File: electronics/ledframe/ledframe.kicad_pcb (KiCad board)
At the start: 2 copper layers, 31 parts, among them CON1 BARREL_JACK, IC1 ATMEGA328P-AUR, P1 PIEZO_IN, P2 FTDI, P3 ICSP, P4 LED_WS2812b, P5 ANT, P6 CONN_01X08, Q1 BSS138, Q2 BSS138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

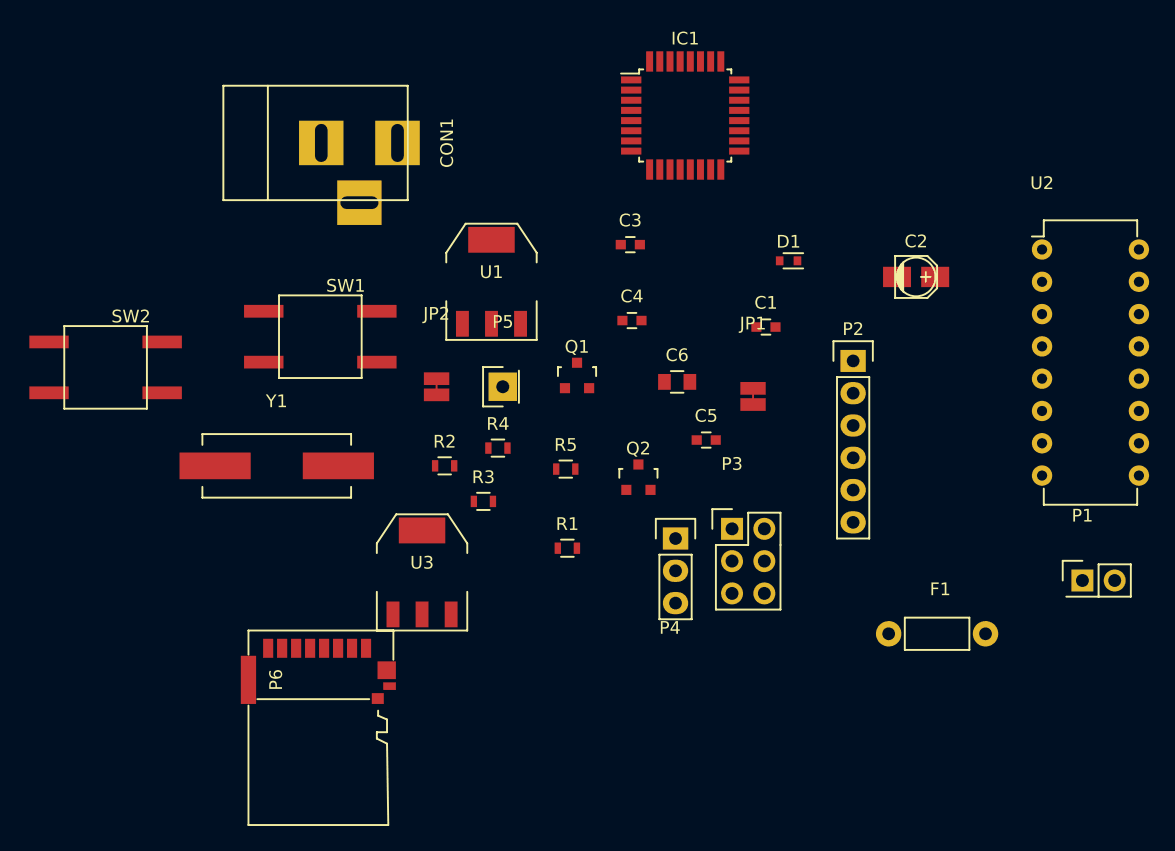
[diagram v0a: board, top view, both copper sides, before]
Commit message: draft layout. still needs rfm69 and resonator footprints
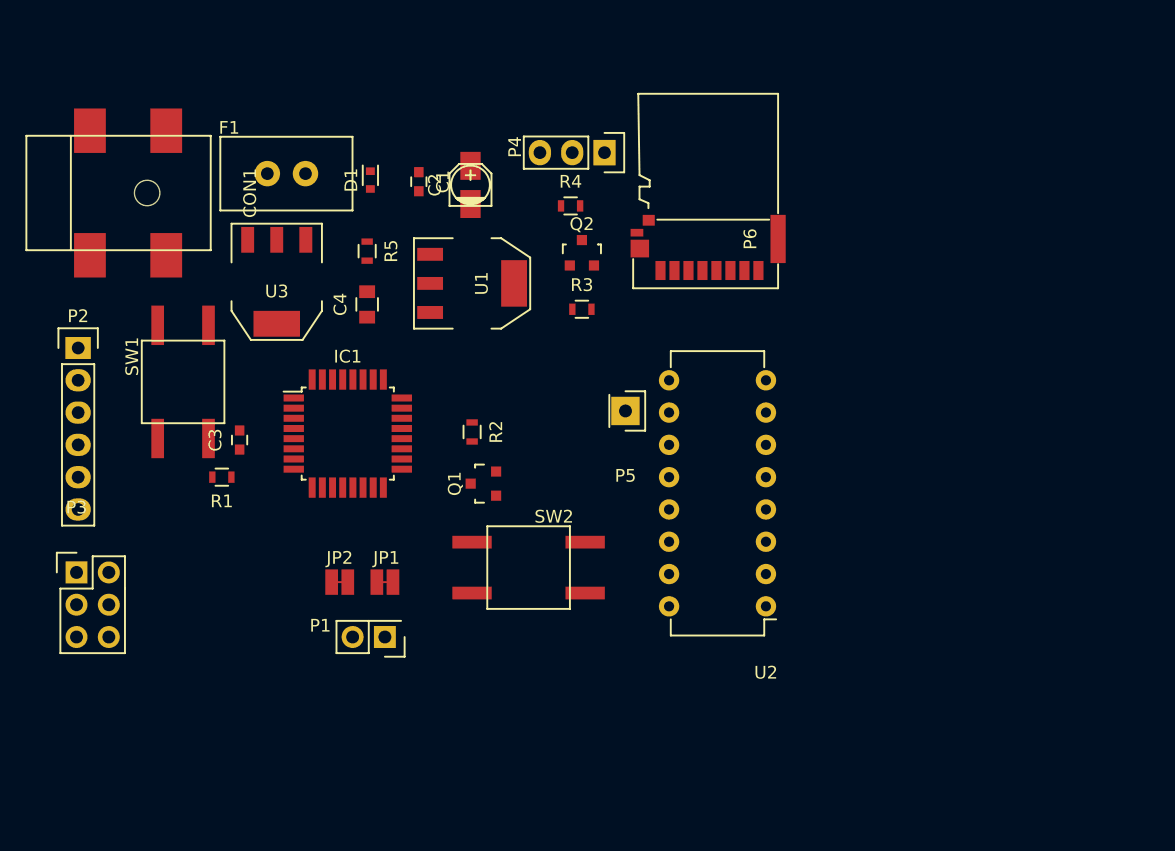
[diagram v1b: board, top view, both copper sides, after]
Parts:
- removed C5: 0.1µF, Capacitors_SMD:C_0603
- removed C6: 1µF, Capacitors_SMD:C_0805
- removed Y1: 16MHz, Crystals:Crystal_HC49-SD_SMD
- C3: value 22pF -> 0.1µF
- C4: value 22pF -> 1µF; footprint Capacitors_SMD:C_0603 -> Capacitors_SMD:C_0805
- CON1: footprint Connect:BARREL_JACK -> local:BARREL_JACK_SMD
- F1: footprint Resistors_ThroughHole:Resistor_Horizontal_RM7mm -> local:Polyfuse_500
- P6: value CONN_01X08 -> MicroSD
- moved P2 61.0 mm to (110.5, 96.9)
- moved F1 59.6 mm to (126.9, 83.2)
- moved P1 55.0 mm to (134.6, 119.6), turned to 180 degrees
- moved P3 51.7 mm to (110.4, 114.6)
- moved P6 42.8 mm to (160.1, 90.8), turned to 180 degrees
- moved SW2 36.8 mm to (145.9, 114.2)
- moved IC1 36.5 mm to (131.7, 103.6)
- moved C2 35.8 mm to (141.4, 84.1), turned to 90 degrees
- moved U2 35.5 mm to (164.6, 117.2), turned to 180 degrees
- moved C3 34.4 mm to (123.2, 104.1), turned to 90 degrees
- moved D1 33.5 mm to (133.5, 83.7), turned to 90 degrees
- moved JP1 33.3 mm to (134.0, 115.3), turned to 90 degrees
- moved P4 30.9 mm to (151.9, 81.5), turned to 270 degrees
- moved C1 29.6 mm to (137.3, 83.8), turned to 270 degrees
- moved R1 27.7 mm to (121.8, 107.1), turned to 180 degrees
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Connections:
- C3 pad 2: GND -> RST
- C4 pad 1: Net-(C4-Pad1) -> +3V3
- IC1 pad 29: Net-(C5-Pad1) -> Net-(C3-Pad1)
- IC1 pad 7: Net-(C4-Pad1) -> Net-(IC1-Pad7)
- IC1 pad 8: Net-(C3-Pad1) -> Net-(IC1-Pad8)
- R1 pad 2: Net-(C5-Pad1) -> Net-(C3-Pad1)
- SW1 pad 1: Net-(C5-Pad1) -> Net-(C3-Pad1)

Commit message: first draft routing
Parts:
- U2: footprint Housings_DIP:DIP-16_W7.62mm -> local:RFM69
- moved Q2 98.2 mm to (78.0, 156.0)
- moved R3 97.9 mm to (78.0, 160.0)
- moved C3 96.5 mm to (52.2, 169.5), turned to 0 degrees
- moved CON1 93.0 mm to (44.0, 146.0)
- moved SW1 92.9 mm to (50.0, 162.0), turned to 0 degrees
- moved P2 92.0 mm to (40.0, 156.0)
- moved R1 91.8 mm to (52.2, 167.0)
- moved D1 91.5 mm to (63.0, 142.0)
- moved P4 90.9 mm to (77.0, 133.0)
- moved C1 90.5 mm to (68.0, 142.0)
- moved U3 90.4 mm to (57.0, 150.0)
- moved F1 90.4 mm to (55.0, 138.0), turned to 270 degrees
- moved R5 90.3 mm to (63.0, 146.0)
- moved C4 90.1 mm to (63.0, 150.0)
- moved U1 90.0 mm to (72.0, 149.0)
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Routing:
- net +3V3: track 0.00 -> 124.3 mm, vias 0 -> 5
- net +5V: track 0.00 -> 97.9 mm
- net MOSI: track 0.00 -> 88.0 mm, vias 0 -> 4
- net SCK: track 0.00 -> 74.8 mm, vias 0 -> 4
- net MISO: track 0.00 -> 73.0 mm, vias 0 -> 2
- net INT0: track 0.00 -> 61.1 mm, vias 0 -> 2
- net Net-(C3-Pad1): track 0.00 -> 45.9 mm, vias 0 -> 2
- net GND: track 0.00 -> 43.3 mm, vias 0 -> 8
- net RADIO_SS: track 0.00 -> 38.4 mm, vias 0 -> 2
- net INT1: track 0.00 -> 37.0 mm, vias 0 -> 2
- net SD_SS: track 0.00 -> 36.8 mm, vias 0 -> 2
- net RX: track 0.00 -> 31.7 mm
- net TX: track 0.00 -> 28.4 mm, vias 0 -> 2
- net LED_DATA: track 0.00 -> 27.8 mm, vias 0 -> 2
- net Net-(CON1-Pad1): track 0.00 -> 24.3 mm
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- added copper zone on B.Cu, net GND
- added copper zone on F.Cu, net GND
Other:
- board outline added: 72 x 52 mm
- net class HI_PWR added: clearance 0.3, trace_width 0.5, via_dia 1.75, via_drill 1
- net class PWR added: clearance 0.2, trace_width 0.25, via_dia 1.75, via_drill 1
- board text added: "LEDframe"
- board text added: "rev1"

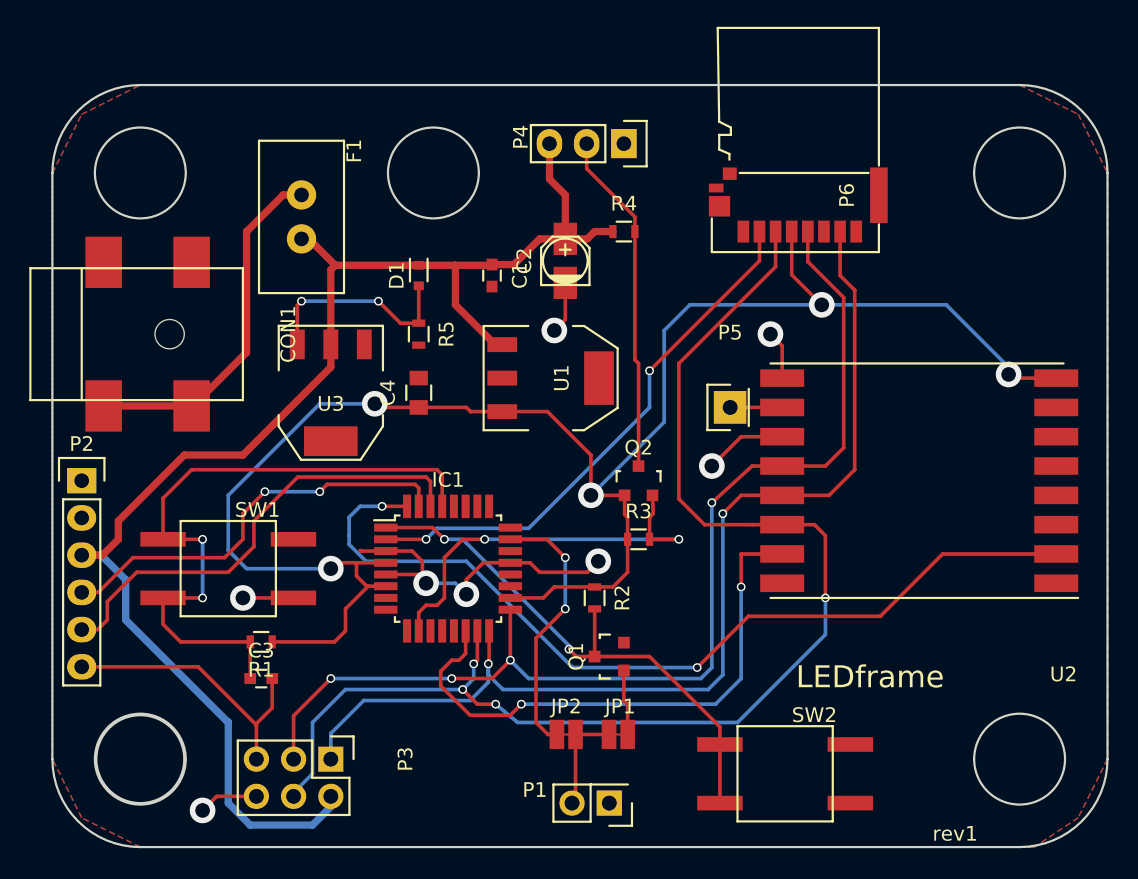
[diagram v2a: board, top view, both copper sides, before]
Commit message: included the missing resonator(!)
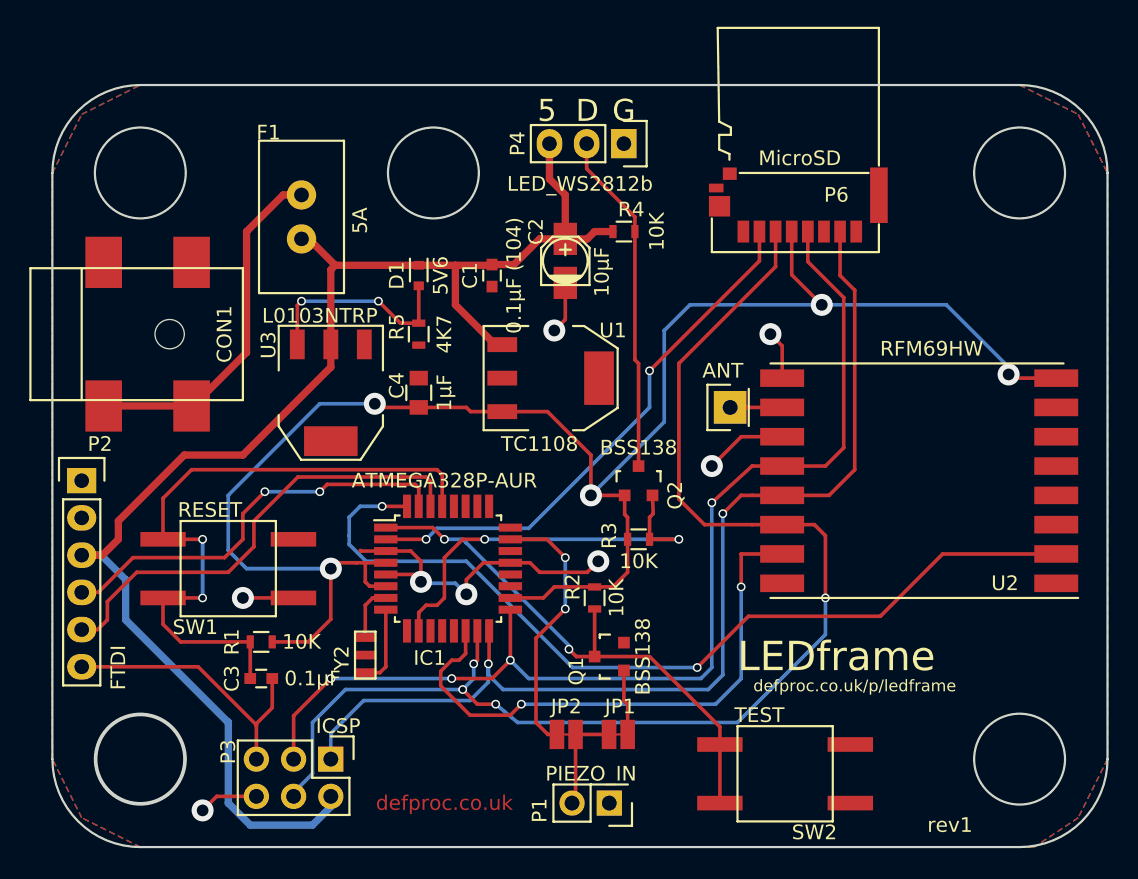
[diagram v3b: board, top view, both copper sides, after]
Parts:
- added Y2: Resonator, local:Resonator_3.2x1.3, F.Cu at (59.4, 169.5)
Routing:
- net Net-(IC1-Pad8): track 0.00 -> 5.47 mm
- net Net-(IC1-Pad7): track 0.00 -> 3.81 mm
- net +3V3: track 124.3 -> 123.0 mm
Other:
- net class PWR: via_dia 1.75 -> 1.5; via_drill 1 -> 0.8
- board text added: "5"
- board text added: "5A"
- board text added: "5V6"
- board text added: "D"
- board text added: "G"
- board text added: "RFM69HW"
- board text added: "defproc.co.uk"
- board text added: "defproc.co.uk/p/ledframe"
